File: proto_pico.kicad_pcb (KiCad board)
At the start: 2 copper layers, 105 parts, among them J1 USB-C Receptacle, J11 Header_2.54mm_1x5, J16 Header_2.54mm_1x5, J2 Screw_Terminal_01x02, J3 Screw_Terminal_01x02, J4 Screw_Terminal_01x02, J6 Header_2.54mm_1x7, J8 Header_2.54mm_1x5, SW1 PTS647, SW2 PTS647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

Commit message: done some routing
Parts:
- moved J4 168.4 mm to (208.0, 51.3)
- moved C19 162.4 mm to (189.2, 132.0)
- moved C20 162.4 mm to (189.2, 134.5)
- moved D4 162.4 mm to (209.3, 139.8)
- moved D5 162.4 mm to (209.3, 142.4)
- moved D6 162.4 mm to (209.3, 145.0)
- moved D7 162.4 mm to (209.3, 147.6)
- moved D8 162.4 mm to (209.3, 150.2)
- moved R19 162.4 mm to (201.2, 132.0)
- moved R20 162.4 mm to (201.2, 134.5)
- moved R21 162.4 mm to (201.2, 137.1)
- moved R28 162.4 mm to (205.2, 132.0)
- moved R29 162.4 mm to (205.2, 134.5)
- moved R31 162.4 mm to (205.2, 139.6)
- moved R32 162.4 mm to (205.2, 142.1)
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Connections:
- J11 pad 1: unconnected-(J11-Pad1) -> /HB_MODE
- J6 pad 1: /SCL -> /MCLK_AUDIO
- J6 pad 2: /SDA -> /LRCLK_AUDIO
- J6 pad 3: /MCLK_AUDIO -> /SCL
- J6 pad 4: /LRCLK_AUDIO -> /SDA
- J6 pad 5: /SCLK_AUDIO -> /SDO_AUDIO
- J6 pad 6: /SDO_AUDIO -> /SDI_AUDIO
- J6 pad 7: /SDI_AUDIO -> /SCLK_AUDIO

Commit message: some updates to schematic and component placement
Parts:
- moved U5 56.5 mm to (164.4, 115.4)
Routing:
- net /QSPI_D3: track 0.00 -> 12.5 mm
- net /QSPI_CLK: track 0.00 -> 11.2 mm
- net +3V3: track 0.00 -> 9.65 mm
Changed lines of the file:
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@@
   )
   (footprint "Memory:SOIC-8_5.23x5.23mm_P1.27mm" (layer "F.Cu")
-    (at 202.942 156.756)
+    (at 164.382 115.443)
     (descr "SOIC, 8 Pin (http://www.winbond.com/resource-files/w25q32jv%20revg%2003272018%20plus.pdf#page=68), generated with kicad-footprint-generator ipc_gullwing_generator.py")
     (tags "SOIC SO")
@@
     )
   )
+  (segment (start 167.982 113.538) (end 168.183751 113.538) (width 0.25) (layer "F.Cu") (net 1))
+  (segment (start 173.989251 119.3435) (end 175.2255 119.3435) (width 0.25) (layer "F.Cu") (net 1))
+  (segment (start 168.183751 113.538) (end 173.989251 119.3435) (width 0.25) (layer "F.Cu") (net 1))
+  (segment (start 168.183751 114.808) (end 173.517751 120.142) (width 0.25) (layer "F.Cu") (net 119))
+  (segment (start 173.517751 120.142) (end 177.292 120.142) (width 0.25) (layer "F.Cu") (net 119))
+  (segment (start 167.982 114.808) (end 168.183751 114.808) (width 0.25) (layer "F.Cu") (net 119))
+  (segment (start 177.508 120.358) (end 177.508 121.08117) (width 0.25) (layer "F.Cu") (net 119))
+  (segment (start 177.292 120.142) (end 177.508 120.358) (width 0.25) (layer "F.Cu") (net 119))
+  (segment (start 172.755751 120.65) (end 177.038 120.65) (width 0.25) (layer "F.Cu") (net 120))
+  (segment (start 177.038 120.65) (end 177.038 120.9365) (width 0.25) (layer "F.Cu") (net 120))
+  (segment (start 167.982 116.078) (end 168.183751 116.078) (width 0.25) (layer "F.Cu") (net 120))
+  (segment (start 168.183751 116.078) (end 172.755751 120.65) (width 0.25) (layer "F.Cu") (net 120))
 )

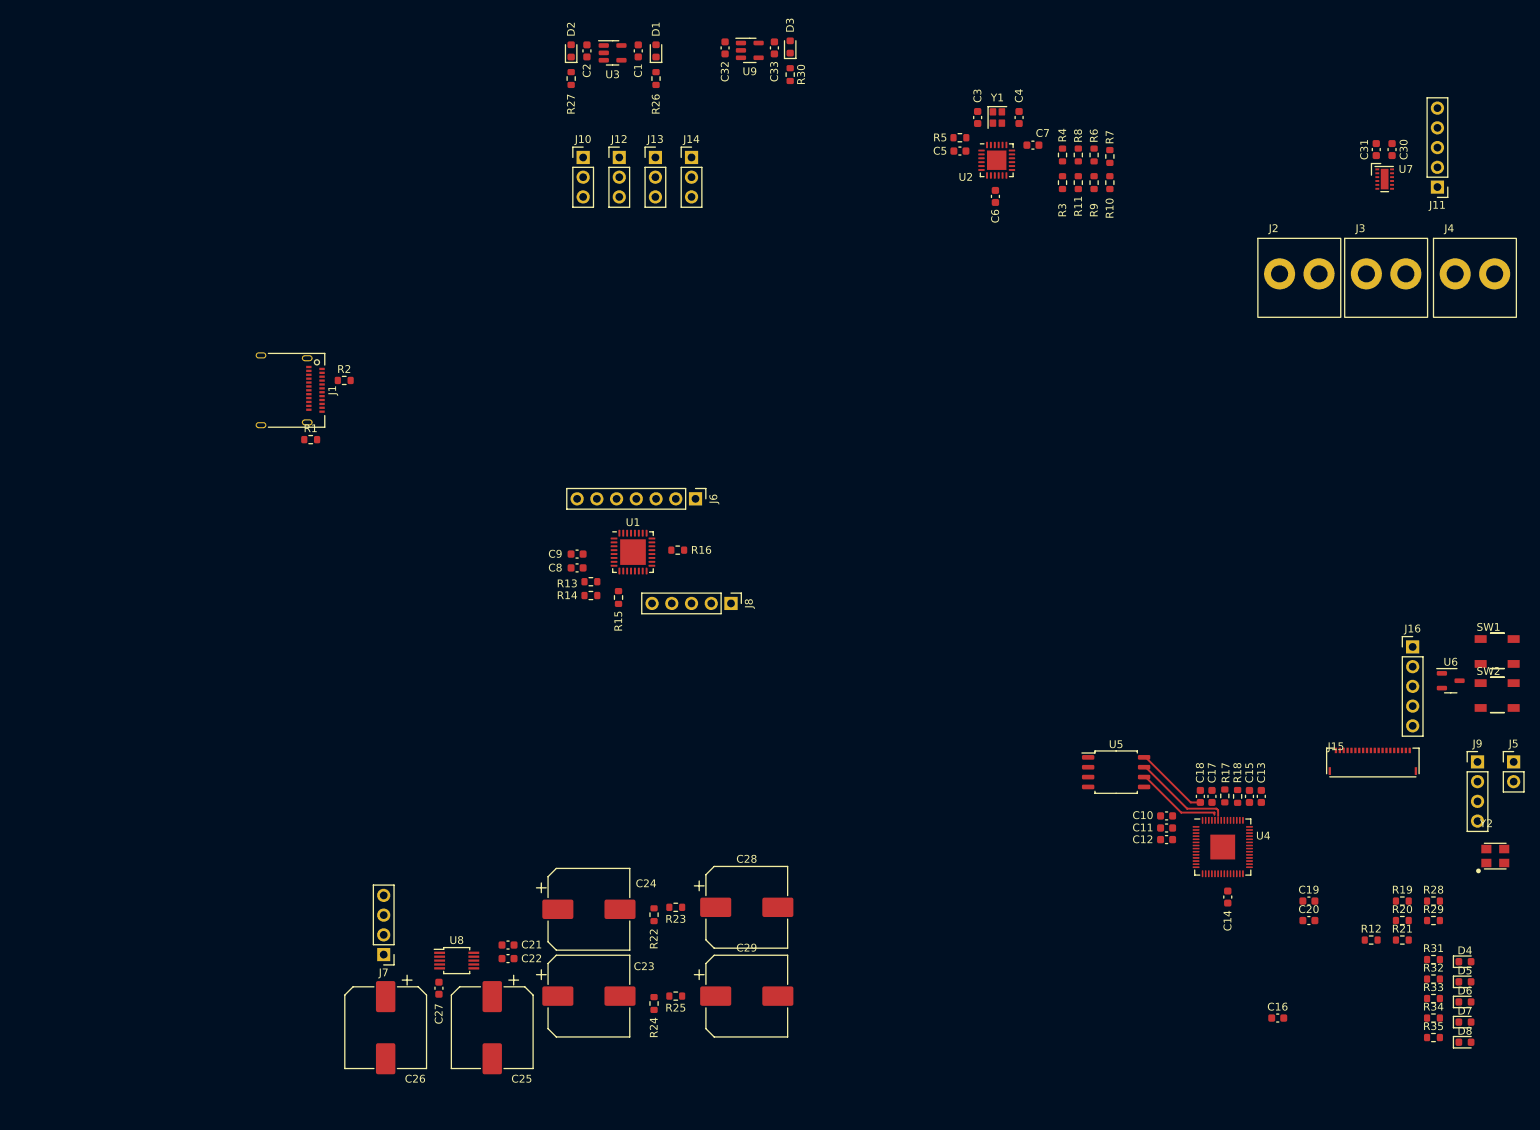
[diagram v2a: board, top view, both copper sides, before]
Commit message: routing done, DRC left
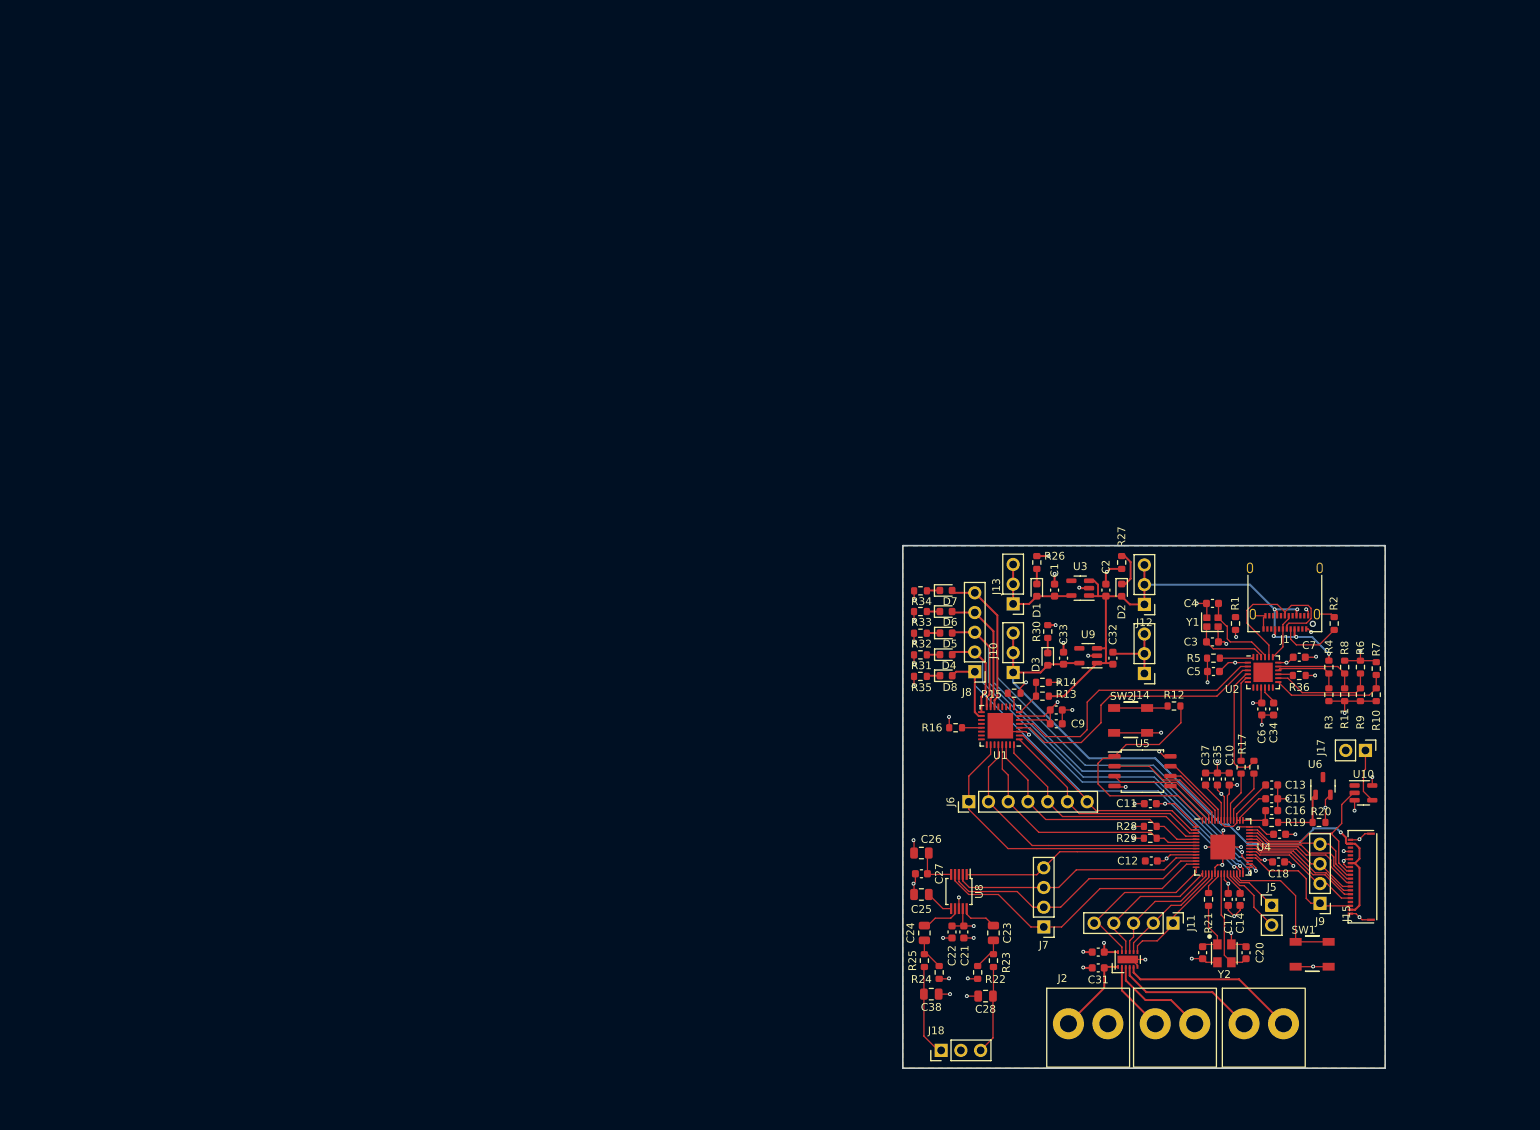
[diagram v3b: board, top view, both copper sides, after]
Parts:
- removed C29: ?, Capasitors:CP_Elec_10x10
- removed J16: Header_2.54mm_1x5, Connectors:PinHeader_1x05_P2.54mm_Vertical
- added C34: 1u, Capasitors:C_0603_1608Metric, F.Cu at (184.7, 107.3)
- added C35: 100n, Capasitors:C_0603_1608Metric, F.Cu at (177.4, 116.3)
- added C36: 100n, Capasitors:C_0603_1608Metric, F.Cu at (185.4, 123.4)
- added C37: 100n, Capasitors:C_0603_1608Metric, F.Cu at (175.9, 116.3)
- added C38: ?, Capasitors:C_0805_2012Metric, F.Cu at (140.6, 144.0)
- added J17: ~, Connectors:PinHeader_1x02_P2.54mm_Vertical, F.Cu at (196.5, 112.6)
- added J18: ~, Connectors:PinHeader_1x03_P2.54mm_Vertical, F.Cu at (141.9, 151.3)
- added R36: 100k, Resistor_SMD:R_0603_1608Metric, F.Cu at (188.0, 103.0)
- added U10: 74LVC1G17, Package_TO_SOT_SMD:SOT-23-5, F.Cu at (196.2, 118.1)
- C23, C24, C25, C26, C28: footprint Capasitors:CP_Elec_10x10 -> Capasitors:C_0805_2012Metric
- moved J1 131.5 mm to (186.1, 92.0), turned to 180 degrees
- moved R2 131.2 mm to (192.4, 96.3), turned to 90 degrees
- moved R1 121.4 mm to (179.8, 96.3), turned to -90 degrees
- moved C31 111.2 mm to (162.1, 140.6), turned to 180 degrees
- moved C30 110.0 mm to (162.1, 138.6), turned to 180 degrees
- moved U7 105.8 mm to (165.9, 139.6), turned to 90 degrees
- moved J11 100.7 mm to (171.7, 134.9), turned to -90 degrees
- moved J2 100.3 mm to (158.2, 147.8)
- moved J3 100.3 mm to (169.4, 147.8)
- moved J4 100.3 mm to (180.8, 147.8)
- moved D2 99.2 mm to (165.1, 92.0), turned to -90 degrees
- moved C2 96.3 mm to (163.1, 92.0), turned to 90 degrees
- moved R27 94.4 mm to (165.1, 88.5), turned to -90 degrees
- moved C32 93.1 mm to (164.0, 100.8), turned to 90 degrees
- moved U3 91.5 mm to (159.8, 91.8), turned to 180 degrees
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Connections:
- C23 pad 1: Net-(U8-AOUTL) -> Net-(U8-AOUTR)
- C24 pad 1: Net-(U8-AOUTR) -> Net-(C24-Pad1)
- C24 pad 2: Net-(C24-Pad2) -> Net-(U8-AOUTL)
- J11 pad 1: /HB_MODE -> /HB_ENABLE_B
- J11 pad 2: /HB_ENABLE_B -> /HB_DIRECTION_B
- J11 pad 3: /HB_DIRECTION_B -> /HB_ENABLE_A
- J11 pad 4: /HB_ENABLE_A -> /HB_DIRECTION_A
- J11 pad 5: /HB_DIRECTION_A -> /HB_MODE
- J9 pad 1: /MIC_D4 -> /MIC_CLK
- J9 pad 2: /MIC_D5 -> /MIC_WS
- J9 pad 3: /MIC_D6 -> /MIC_D3
- J9 pad 4: /MIC_D7 -> /MIC_D6
- R22 pad 2: Net-(C24-Pad2) -> Net-(C23-Pad2)
- R23 pad 2: Net-(C24-Pad2) -> Net-(C23-Pad2)
- R24 pad 1: Net-(C23-Pad2) -> Net-(C24-Pad1)
- R25 pad 2: Net-(C23-Pad2) -> Net-(C24-Pad1)
- R28 pad 1: /SCL -> /SDA
- R29 pad 1: /SDA -> /SCL
- U2 pad 10: (no net) -> Net-(U2-CRFILT)
- U2 pad 15: unconnected-(U2-RESET_N-Pad15) -> Net-(U2-RESET_N)
- U2 pad 2: /PICO_D- -> /AUDIO_D-
- U2 pad 23: (no net) -> unconnected-(U2-PLLFILT-Pad23)
- U2 pad 3: /PICO_D+ -> /AUDIO_D+
- U2 pad 4: /AUDIO_D- -> /PICO_D-
- U2 pad 5: /AUDIO_D+ -> /PICO_D+
- U4 pad 14: /HB_DIRECTION_A -> /HB_MODE
- U4 pad 15: /HB_ENABLE_A -> /HB_DIRECTION_A
- U4 pad 16: /HB_DIRECTION_B -> /HB_ENABLE_A
- U4 pad 17: /HB_ENABLE_B -> /HB_DIRECTION_B
- U4 pad 18: /HB_MODE -> /HB_ENABLE_B
- U4 pad 2: /SCL -> /SCLK_AUDIO
- U4 pad 3: /SDA -> /SDI_AUDIO
- U4 pad 4: /MCLK_AUDIO -> /SDO_AUDIO
- U4 pad 5: /LRCLK_AUDIO -> /SDA
- U4 pad 6: /SCLK_AUDIO -> /SCL
- U4 pad 7: /SDO_AUDIO -> /LRCLK_AUDIO
- U4 pad 8: /SDI_AUDIO -> /MCLK_AUDIO
- U6 pad 3: (no net) -> unconnected-(U6-NC-Pad3)
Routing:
- net GND: track 0.00 -> 142.1 mm, vias 0 -> 56
- net +3V3: track 9.65 -> 94.8 mm, vias 0 -> 22
- net +2V8: track 0.00 -> 81.2 mm, vias 0 -> 1
- net /AUDIO_GPIO4: track 0.00 -> 73.7 mm, vias 0 -> 1
- net +5V: track 0.00 -> 72.7 mm, vias 0 -> 5
- net /AUDIO_GPIO3: track 0.00 -> 71.5 mm, vias 0 -> 1
- net /AUDIO_GPIO2: track 0.00 -> 65.3 mm, vias 0 -> 1
- net /AUDIO_GPIO1: track 0.00 -> 60.0 mm, vias 0 -> 1
- net /AUDIO_GPIO0: track 0.00 -> 55.5 mm, vias 0 -> 1
- net /MCLK_AUDIO: track 0.00 -> 40.8 mm
- net /MCLK_DAC: track 0.00 -> 37.7 mm
- net /LRCLK_AUDIO: track 0.00 -> 36.9 mm
- net /AUDIO_D-: track 0.00 -> 35.9 mm
- net /AUDIO_D+: track 0.00 -> 35.4 mm
- net /LRCLK_DAC: track 0.00 -> 35.3 mm
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- added copper zone on B.Cu, net +3V3
- added copper zone on In1.Cu, net GND
- added copper zone on In2.Cu, net GND
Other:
- board outline added: 62.1 x 67.3 mm
- copper layers 2 -> 4

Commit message: update to pcb
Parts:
- moved J18 3.71 mm to (145.6, 151.1)
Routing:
- net +1V1: track 22.8 -> 35.6 mm, vias 0 -> 2
- net /AOUTL: track 11.9 -> 14.7 mm
- net +3V3: track 94.8 -> 93.3 mm
- net GND: track 142.1 -> 143.5 mm, vias 56 -> 61
